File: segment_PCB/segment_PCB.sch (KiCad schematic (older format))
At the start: 165 parts, among them J1 USB_C_Receptacle_USB2.0, J2 AVR-ISP-6, SW1 SW_Push, SW10 SW_Push, SW11 SW_Push, SW12 SW_Push, SW13 SW_Push, SW14 SW_Push, SW15 SW_Push, SW16 SW_Push, SW17 SW_Push, SW18 SW_Push, SW19 SW_Push, SW2 SW_Push, SW20 SW_Push, SW21 SW_Push, SW22 SW_Push, SW23 SW_Push, SW24 SW_Push, SW25 SW_Push, SW26 SW_Push, SW27 SW_Push, SW28 SW_Push, SW29 SW_Push, SW3 SW_Push, SW30 SW_Push, SW31 SW_Push, SW32 SW_Push, SW33 SW_Push, SW34 SW_Push, SW35 SW_Push, SW36 SW_Push, SW37 SW_Push, SW38 SW_Push, SW39 SW_Push, SW4 SW_Push, SW40 SW_Push, SW41 SW_Push, SW42 SW_Push, SW43 SW_Push, SW44 SW_Push, SW45 SW_Push, SW46 SW_Push, SW47 SW_Push, SW48 SW_Push, SW49 SW_Push, SW5 SW_Push, SW50 SW_Push, SW51 SW_Push, SW52 SW_Push, SW53 SW_Push, SW54 SW_Push, SW55 SW_Push, SW56 SW_Push, SW57 SW_Push, SW58 SW_Push, SW59 SW_Push, SW6 SW_Push, SW60 SW_Push, SW61 SW_Push, SW62 SW_Push, SW63 SW_Push, SW64 SW_Push, SW65 SW_Push, SW66 SW_Push, SW67 SW_Push, SW68 SW_Push, SW69 SW_Push, SW7 SW_Push, SW70 SW_Push, SW71 SW_Push, SW8 SW_Push, SW9 SW_Push, U1 ATtiny2313A-PU, U2 74HC238, U3 74HC238, Y1 12MHz

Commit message: Updated schematic and library names
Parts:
- removed U2, U3: 74HC238, symbol keyboard-parts:74HC238
- added U? (x2): 74HC238, symbol Segment_Parts:74HC238
- C1, C3, C4, C5, C6, C7: footprint (none) -> Capacitor_THT:C_Disc_D3.0mm_W1.6mm_P2.50mm
- D1, D2: footprint (none) -> Diode_THT:D_DO-35_SOD27_P7.62mm_Horizontal
- D3, D4: footprint (none) -> LED_THT:LED_D5.0mm
- J2: footprint (none) -> Connector_PinHeader_2.54mm:PinHeader_2x03_P2.54mm_Vertical
- R1, R2, R3, R4, R5, R6, R7: footprint (none) -> Resistor_THT:R_Axial_DIN0204_L3.6mm_D1.6mm_P5.08mm_Horizontal
- Y1: footprint (none) -> Crystal:Crystal_HC52-6mm_Vertical
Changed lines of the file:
@@
 F 0 "Y1" V 3096 7519 50  0000 R CNN
 F 1 "12MHz" V 3005 7519 50  0000 R CNN
-F 2 "" H 3050 7650 50  0001 C CNN
+F 2 "Crystal:Crystal_HC52-6mm_Vertical" H 3050 7650 50  0001 C CNN
 F 3 "~" H 3050 7650 50  0001 C CNN
 	1    3050 7650
@@
 F 0 "C7" V 2598 7850 50  0000 C CNN
 F 1 "22p" V 2689 7850 50  0000 C CNN
-F 2 "" H 2888 7700 50  0001 C CNN
+F 2 "Capacitor_THT:C_Disc_D3.0mm_W1.6mm_P2.50mm" H 2888 7700 50  0001 C CNN
 F 3 "~" H 2850 7850 50  0001 C CNN
 	1    2850 7850
@@
 F 0 "C6" V 2598 7450 50  0000 C CNN
 F 1 "22p" V 2689 7450 50  0000 C CNN
-F 2 "" H 2888 7300 50  0001 C CNN
+F 2 "Capacitor_THT:C_Disc_D3.0mm_W1.6mm_P2.50mm" H 2888 7300 50  0001 C CNN
 F 3 "~" H 2850 7450 50  0001 C CNN
 	1    2850 7450
@@
 F 0 "R5" H 6420 7346 50  0000 L CNN
 F 1 "R" H 6420 7255 50  0000 L CNN
-F 2 "" V 6280 7300 50  0001 C CNN
+F 2 "Resistor_THT:R_Axial_DIN0204_L3.6mm_D1.6mm_P5.08mm_Horizontal" V 6280 7300 50  0001 C CNN
 F 3 "~" H 6350 7300 50  0001 C CNN
 	1    6350 7300
@@
 F 0 "D3" V 5339 7232 50  0000 R CNN
 F 1 "LED" V 5248 7232 50  0000 R CNN
-F 2 "" H 5300 7350 50  0001 C CNN
+F 2 "LED_THT:LED_D5.0mm" H 5300 7350 50  0001 C CNN
 F 3 "~" H 5300 7350 50  0001 C CNN
 	1    5300 7350
@@
 F 0 "R6" H 5370 7796 50  0000 L CNN
 F 1 "R" H 5370 7705 50  0000 L CNN
-F 2 "" V 5230 7750 50  0001 C CNN
+F 2 "Resistor_THT:R_Axial_DIN0204_L3.6mm_D1.6mm_P5.08mm_Horizontal" V 5230 7750 50  0001 C CNN
 F 3 "~" H 5300 7750 50  0001 C CNN
 	1    5300 7750
@@
 F 0 "C3" H 6750 1500 50  0000 L CNN
 F 1 "100n" H 6750 1300 50  0000 L CNN
-F 2 "" H 6738 1250 50  0001 C CNN
+F 2 "Capacitor_THT:C_Disc_D3.0mm_W1.6mm_P2.50mm" H 6738 1250 50  0001 C CNN
 F 3 "~" H 6700 1400 50  0001 C CNN
 	1    6700 1400
@@
 F 0 "C1" H 2965 1496 50  0000 L CNN
 F 1 "4.7u" H 2965 1405 50  0000 L CNN
-F 2 "" H 2888 1300 50  0001 C CNN
+F 2 "Capacitor_THT:C_Disc_D3.0mm_W1.6mm_P2.50mm" H 2888 1300 50  0001 C CNN
 F 3 "~" H 2850 1450 50  0001 C CNN
 	1    2850 1450
@@
 F 0 "R2" H 2575 2450 50  0000 R CNN
 F 1 "1.5K" H 2575 2750 50  0000 R CNN
-F 2 "" V 2530 2600 50  0001 C CNN
+F 2 "Resistor_THT:R_Axial_DIN0204_L3.6mm_D1.6mm_P5.08mm_Horizontal" V 2530 2600 50  0001 C CNN
 F 3 "~" H 2600 2600 50  0001 C CNN
 	1    2600 2600
@@
 F 0 "R1" H 2325 2450 50  0000 R CNN
 F 1 "1.5K" H 2325 2750 50  0000 R CNN
-F 2 "" V 2280 2600 50  0001 C CNN
+F 2 "Resistor_THT:R_Axial_DIN0204_L3.6mm_D1.6mm_P5.08mm_Horizontal" V 2280 2600 50  0001 C CNN
 F 3 "~" H 2350 2600 50  0001 C CNN
 	1    2350 2600
@@
 F 0 "R4" V 3375 2450 50  0000 C CNN
 F 1 "1.5K" V 3375 2275 50  0000 C CNN
-F 2 "" V 3230 2350 50  0001 C CNN
+F 2 "Resistor_THT:R_Axial_DIN0204_L3.6mm_D1.6mm_P5.08mm_Horizontal" V 3230 2350 50  0001 C CNN
 F 3 "~" H 3300 2350 50  0001 C CNN
 	1    3300 2350
@@
 F 0 "R3" V 3375 2250 50  0000 C CNN
 F 1 "1.5K" V 3375 2075 50  0000 C CNN
-F 2 "" V 3230 2150 50  0001 C CNN
+F 2 "Resistor_THT:R_Axial_DIN0204_L3.6mm_D1.6mm_P5.08mm_Horizontal" V 3230 2150 50  0001 C CNN
 F 3 "~" H 3300 2150 50  0001 C CNN
 	1    3300 2150
@@
 F 0 "D2" V 3000 2625 50  0000 L CNN
 F 1 "3.6V" V 3200 2625 50  0000 L CNN
-F 2 "" H 3100 2600 50  0001 C CNN
+F 2 "Diode_THT:D_DO-35_SOD27_P7.62mm_Horizontal" H 3100 2600 50  0001 C CNN
 F 3 "~" H 3100 2600 50  0001 C CNN
 	1    3100 2600
@@
 F 0 "D1" V 2750 2625 50  0000 L CNN
 F 1 "3.6V" V 2950 2625 50  0000 L CNN
-F 2 "" H 2850 2600 50  0001 C CNN
+F 2 "Diode_THT:D_DO-35_SOD27_P7.62mm_Horizontal" H 2850 2600 50  0001 C CNN
 F 3 "~" H 2850 2600 50  0001 C CNN
 	1    2850 2600
@@
 F 0 "C5" H 5515 5046 50  0000 L CNN
 F 1 "100n" H 5515 4955 50  0000 L CNN
-F 2 "" H 5438 4850 50  0001 C CNN
+F 2 "Capacitor_THT:C_Disc_D3.0mm_W1.6mm_P2.50mm" H 5438 4850 50  0001 C CNN
 F 3 "~" H 5400 5000 50  0001 C CNN
 	1    5400 5000
@@
 F 0 "C4" H 3065 4996 50  0000 L CNN
 F 1 "100n" H 3065 4905 50  0000 L CNN
-F 2 "" H 2988 4800 50  0001 C CNN
+F 2 "Capacitor_THT:C_Disc_D3.0mm_W1.6mm_P2.50mm" H 2988 4800 50  0001 C CNN
 F 3 "~" H 2950 4950 50  0001 C CNN
 	1    2950 4950
@@
 $EndComp
 $Comp
-L keyboard-parts:74HC238 U3
-U 1 1 5F1E5469
-P 4500 5450
-F 0 "U3" H 4500 5500 50  0000 C CNN
-F 1 "74HC238" H 4750 4950 50  0000 C CNN
-F 2 "" H 4500 5450 50  0001 C CNN
-F 3 "http://www.ti.com/lit/ds/symlink/cd74hc237.pdf" H 4500 5450 50  0001 C CNN
-	1    4500 5450
-	1    0    0    -1
-$EndComp
-$Comp
-L keyboard-parts:74HC238 U2
-U 1 1 5F1E2086
-P 2100 5400
-F 0 "U2" H 2100 5450 50  0000 C CNN
-F 1 "74HC238" H 2350 4900 50  0000 C CNN
-F 2 "" H 2100 5400 50  0001 C CNN
-F 3 "http://www.ti.com/lit/ds/symlink/cd74hc237.pdf" H 2100 5400 50  0001 C CNN
-	1    2100 5400
-	1    0    0    -1
-$EndComp
-$Comp
 L power:GND #PWR028
 U 1 1 5F22179F
@@
 F 0 "J2" H 1550 7750 50  0000 R CNN
 F 1 "AVR-ISP-6" H 1950 7300 50  0000 R CNN
-F 2 "" V 1300 7750 50  0001 C CNN
+F 2 "Connector_PinHeader_2.54mm:PinHeader_2x03_P2.54mm_Vertical" V 1300 7750 50  0001 C CNN
 F 3 " ~" H 275 7150 50  0001 C CNN
 	1    1550 7700
@@
 F 0 "D4" V 4539 7232 50  0000 R CNN
 F 1 "LED" V 4448 7232 50  0000 R CNN
-F 2 "" H 4500 7350 50  0001 C CNN
+F 2 "LED_THT:LED_D5.0mm" H 4500 7350 50  0001 C CNN
 F 3 "~" H 4500 7350 50  0001 C CNN
 	1    4500 7350
@@
 F 0 "R7" H 4570 7796 50  0000 L CNN
 F 1 "R" H 4570 7705 50  0000 L CNN
-F 2 "" V 4430 7750 50  0001 C CNN
+F 2 "Resistor_THT:R_Axial_DIN0204_L3.6mm_D1.6mm_P5.08mm_Horizontal" V 4430 7750 50  0001 C CNN
 F 3 "~" H 4500 7750 50  0001 C CNN
 	1    4500 7750
@@
 Wire Bus Line
 	8750 1000 15350 1000
+$Comp
+L Segment_Parts:74HC238 U?
+U 1 1 5F2E3F93
+P 4500 5450
+F 0 "U?" H 4500 5450 50  0000 C CNN
+F 1 "74HC238" H 4750 4950 50  0000 C CNN
+F 2 "" H 4500 5450 50  0001 C CNN
+F 3 "http://www.ti.com/lit/ds/symlink/cd74hc237.pdf" H 4500 5450 50  0001 C CNN
+	1    4500 5450
+	1    0    0    -1
+$EndComp
+$Comp
+L Segment_Parts:74HC238 U?
+U 1 1 5F2E78E3
+P 2100 5400
+F 0 "U?" H 2100 5400 50  0000 C CNN
+F 1 "74HC238" H 2350 4900 50  0000 C CNN
+F 2 "" H 2100 5400 50  0001 C CNN
+F 3 "http://www.ti.com/lit/ds/symlink/cd74hc237.pdf" H 2100 5400 50  0001 C CNN
+	1    2100 5400
+	1    0    0    -1
+$EndComp
 $EndSCHEMATC

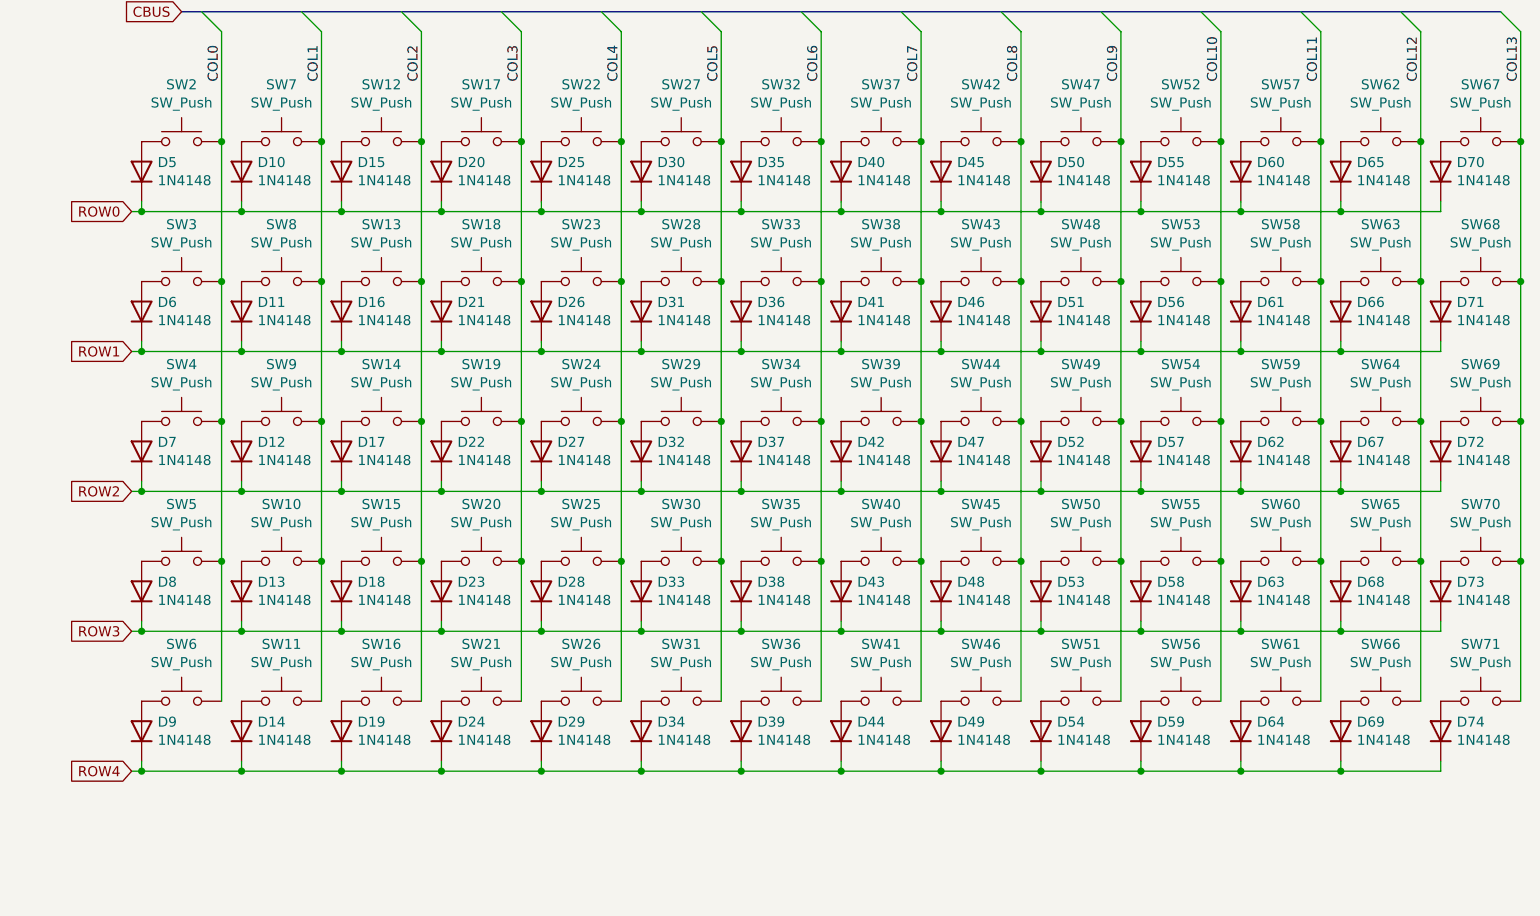
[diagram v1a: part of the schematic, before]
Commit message: Updated switch matrix
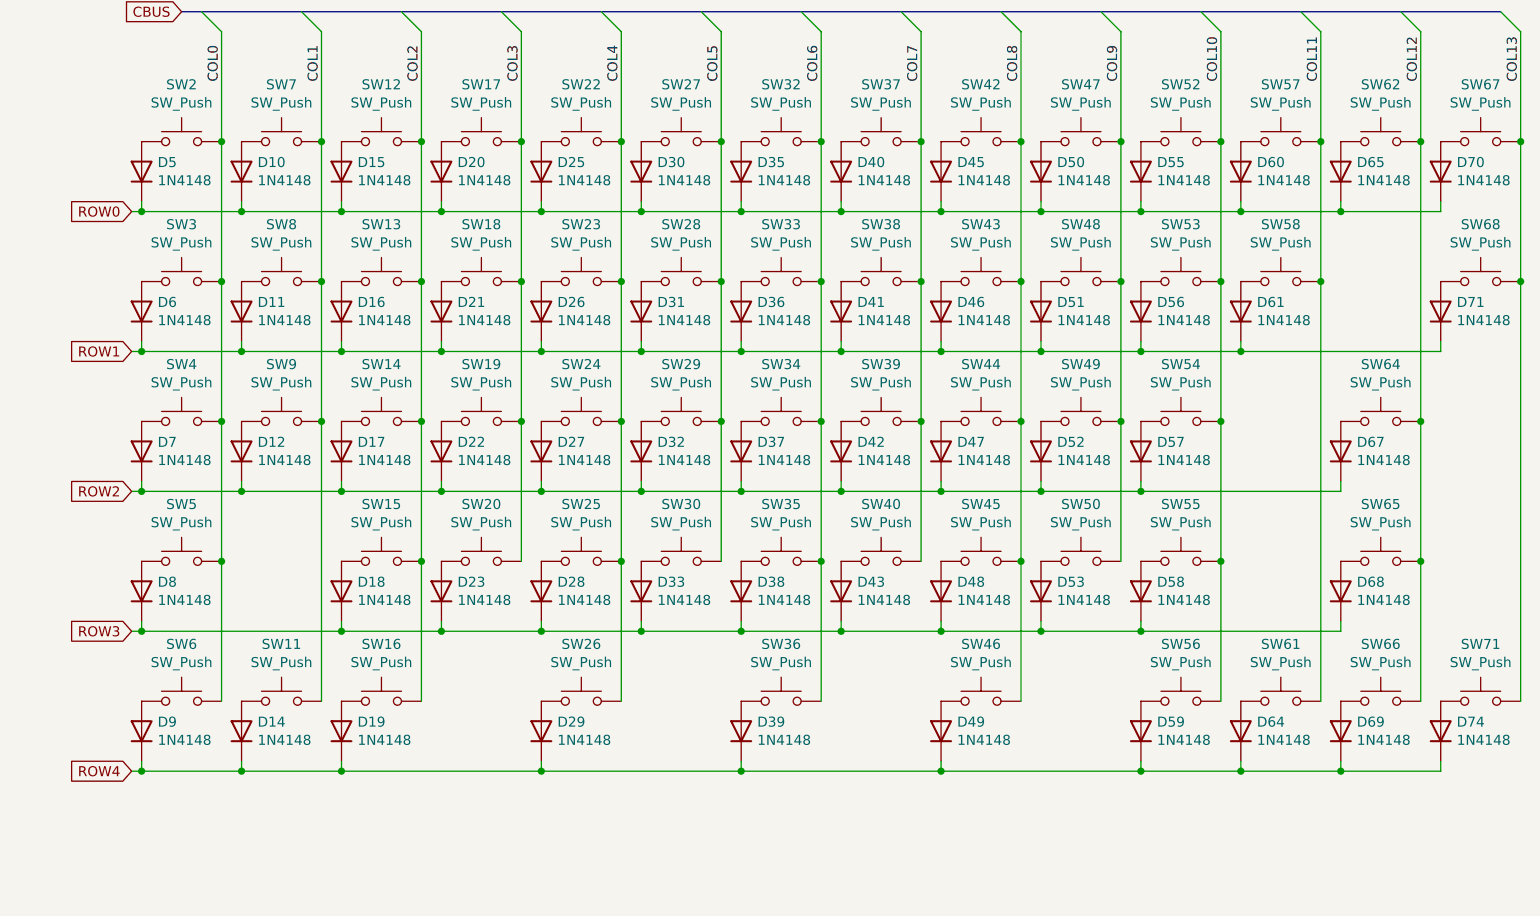
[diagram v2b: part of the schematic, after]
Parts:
- removed D13, D24, D34, D44, D54, D62, D63, D66, D72, D73: 1N4148, symbol Device:D
- removed SW10, SW21, SW31, SW41, SW51, SW59, SW60, SW63, SW69, SW70: SW_Push, symbol Switch:SW_Push

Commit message: added .gitignore
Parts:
- added C?: 100n, Capacitor_THT:C_Disc_D3.0mm_W1.6mm_P2.50mm, symbol Device:C
- added U?: 74HC238, symbol Segment_Parts:74HC238
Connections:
- net COL10: now also U?.13 (Y2)
- net COL11: now also U?.12 (Y3)
- net COL12: now also U?.11 (Y4)
- net COL13: now also U?.10 (Y5)
- net COL8: now also U?.15 (Y0)
- net COL9: now also U?.14 (Y1)
- net GND: now also C?.2, U?.4 (~E1), U?.5 (~E2), U?.8 (GND)
- net SEL0: now also U?.1 (A0)
- net SEL1: now also U?.2 (A1)
- net SEL2: now also U?.3 (A2)
- net SEL3: now also U?.6 (E3)
- net VCC: now also C?.1, U?.16 (VCC)
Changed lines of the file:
@@
 Text GLabel 1400 4800 1    50   Input ~ 0
 SBUS
-Text GLabel 5250 5750 3    50   Input ~ 0
+Text GLabel 5250 6050 3    50   Input ~ 0
 CBUS
 Wire Wire Line
@@
 Text GLabel 8500 4800 0    50   Input ~ 0
 ROW4
-NoConn ~ 4900 5650
-NoConn ~ 4900 5750
 $Comp
 L Device:LED D4
@@
 $Comp
 L Segment_Parts:74HC238 U?
-U 1 1 5F2E3F93
-P 4500 5450
-F 0 "U?" H 4500 5450 50  0000 C CNN
-F 1 "74HC238" H 4750 4950 50  0000 C CNN
-F 2 "" H 4500 5450 50  0001 C CNN
-F 3 "http://www.ti.com/lit/ds/symlink/cd74hc237.pdf" H 4500 5450 50  0001 C CNN
-	1    4500 5450
-	1    0    0    -1
-$EndComp
-$Comp
-L Segment_Parts:74HC238 U?
 U 1 1 5F2E78E3
 P 2100 5400
@@
 	1    0    0    -1
 $EndComp
-Wire Bus Line
-	3700 4850 3700 5650
-Wire Bus Line
-	1400 4800 1400 5400
-Wire Bus Line
-	6550 1650 6550 2050
-Wire Bus Line
-	5250 5150 5250 5750
-Wire Bus Line
-	2800 5100 2800 5900
-Wire Bus Line
-	8750 1000 15350 1000
 Wire Wire Line
 	9450 3050 9450 4450
@@
 Wire Wire Line
 	15450 2350 15450 4450
+Text GLabel 5850 4850 1    50   Input ~ 0
+SBUS
+Text GLabel 7400 5750 3    50   Input ~ 0
+CBUS
+Wire Wire Line
+	6650 4800 7550 4800
+Wire Wire Line
+	7550 4800 7550 4850
+Entry Wire Line
+	7300 5550 7400 5650
+Entry Wire Line
+	7300 5450 7400 5550
+Entry Wire Line
+	7300 5350 7400 5450
+Entry Wire Line
+	7300 5250 7400 5350
+Entry Wire Line
+	7300 5150 7400 5250
+Entry Wire Line
+	7300 5050 7400 5150
+Wire Wire Line
+	7050 5550 7300 5550
+Wire Wire Line
+	7050 5450 7300 5450
+Wire Wire Line
+	7050 5350 7300 5350
+Wire Wire Line
+	7050 5250 7300 5250
+Wire Wire Line
+	7050 5150 7300 5150
+Wire Wire Line
+	7050 5050 7300 5050
+Text Label 7050 5550 0    50   ~ 0
+COL13
+Text Label 7050 5450 0    50   ~ 0
+COL12
+Text Label 7050 5350 0    50   ~ 0
+COL11
+Text Label 7050 5250 0    50   ~ 0
+COL10
+Text Label 7050 5150 0    50   ~ 0
+COL9
+Text Label 7050 5050 0    50   ~ 0
+COL8
+Wire Wire Line
+	5950 5250 6250 5250
+Wire Wire Line
+	5950 5150 6250 5150
+Wire Wire Line
+	5950 5050 6250 5050
+Entry Wire Line
+	5850 5150 5950 5250
+Entry Wire Line
+	5850 5050 5950 5150
+Entry Wire Line
+	5850 4950 5950 5050
+Entry Wire Line
+	5850 5650 5950 5750
+Wire Wire Line
+	5950 5750 6250 5750
+Connection ~ 6000 5650
+Wire Wire Line
+	6000 5550 6250 5550
+Wire Wire Line
+	6000 5650 6000 5550
+Wire Wire Line
+	6000 5650 6250 5650
+Wire Wire Line
+	6000 5950 6000 5650
+Text Label 6250 5750 2    50   ~ 0
+SEL3
+Text Label 6250 5250 2    50   ~ 0
+SEL2
+Text Label 6250 5150 2    50   ~ 0
+SEL1
+Text Label 6250 5050 2    50   ~ 0
+SEL0
+Connection ~ 6650 4800
+Wire Wire Line
+	6650 4850 6650 4800
+Wire Wire Line
+	6650 4800 6650 4750
+$Comp
+L power:GND #PWR?
+U 1 1 5FB14020
+P 7550 5150
+F 0 "#PWR?" H 7550 4900 50  0001 C CNN
+F 1 "GND" H 7555 4977 50  0000 C CNN
+F 2 "" H 7550 5150 50  0001 C CNN
+F 3 "" H 7550 5150 50  0001 C CNN
+	1    7550 5150
+	1    0    0    -1
+$EndComp
+$Comp
+L Device:C C?
+U 1 1 5FB14026
+P 7550 5000
+F 0 "C?" H 7665 5046 50  0000 L CNN
+F 1 "100n" H 7665 4955 50  0000 L CNN
+F 2 "Capacitor_THT:C_Disc_D3.0mm_W1.6mm_P2.50mm" H 7588 4850 50  0001 C CNN
+F 3 "~" H 7550 5000 50  0001 C CNN
+	1    7550 5000
+	1    0    0    -1
+$EndComp
+$Comp
+L power:GND #PWR?
+U 1 1 5FB1402C
+P 6000 5950
+F 0 "#PWR?" H 6000 5700 50  0001 C CNN
+F 1 "GND" H 6005 5777 50  0000 C CNN
+F 2 "" H 6000 5950 50  0001 C CNN
+F 3 "" H 6000 5950 50  0001 C CNN
+	1    6000 5950
+	1    0    0    -1
+$EndComp
+$Comp
+L power:VCC #PWR?
+U 1 1 5FB14032
+P 6650 4750
+F 0 "#PWR?" H 6650 4600 50  0001 C CNN
+F 1 "VCC" H 6665 4923 50  0000 C CNN
+F 2 "" H 6650 4750 50  0001 C CNN
+F 3 "" H 6650 4750 50  0001 C CNN
+	1    6650 4750
+	1    0    0    -1
+$EndComp
+$Comp
+L power:GND #PWR?
+U 1 1 5FB14038
+P 6650 5950
+F 0 "#PWR?" H 6650 5700 50  0001 C CNN
+F 1 "GND" H 6655 5777 50  0000 C CNN
+F 2 "" H 6650 5950 50  0001 C CNN
+F 3 "" H 6650 5950 50  0001 C CNN
+	1    6650 5950
+	1    0    0    -1
+$EndComp
+NoConn ~ 7050 5650
+NoConn ~ 7050 5750
+$Comp
+L Segment_Parts:74HC238 U?
+U 1 1 5FB14040
+P 6650 5450
+F 0 "U?" H 6650 5450 50  0000 C CNN
+F 1 "74HC238" H 6900 4950 50  0000 C CNN
+F 2 "" H 6650 5450 50  0001 C CNN
+F 3 "http://www.ti.com/lit/ds/symlink/cd74hc237.pdf" H 6650 5450 50  0001 C CNN
+	1    6650 5450
+	1    0    0    -1
+$EndComp
+$Comp
+L Segment_Parts:74HC238 U?
+U 1 1 5F2E3F93
+P 4500 5450
+F 0 "U?" H 4500 5450 50  0000 C CNN
+F 1 "74HC238" H 4750 4950 50  0000 C CNN
+F 2 "" H 4500 5450 50  0001 C CNN
+F 3 "http://www.ti.com/lit/ds/symlink/cd74hc237.pdf" H 4500 5450 50  0001 C CNN
+	1    4500 5450
+	1    0    0    -1
+$EndComp
+Wire Bus Line
+	3700 4850 3700 5650
+Wire Bus Line
+	1400 4800 1400 5400
+Wire Bus Line
+	6550 1650 6550 2050
+Wire Bus Line
+	5850 4850 5850 5650
+Wire Bus Line
+	5250 5150 5250 5750
+Wire Bus Line
+	7400 5150 7400 5750
+Wire Bus Line
+	2800 5100 2800 5900
+Wire Bus Line
+	8750 1000 15350 1000
 $EndSCHEMATC
